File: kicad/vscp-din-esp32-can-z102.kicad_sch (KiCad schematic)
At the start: 39 parts, among them J1 Conn_01x05, J2 Conn_01x02, J3 Conn_01x06, J4 Conn_01x04, J5 Conn_01x04, J6 Conn_01x03, J7 Conn_01x05, J8 Conn_01x02, J9 Conn_01x02, U1 ESP32-C3-WROOM-02-N4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

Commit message: Added code of conduct
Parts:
- U1: DESCRIPTION WiFi Modules (802.11) (Engineering Samples) SMD module, ESP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 -> (none)

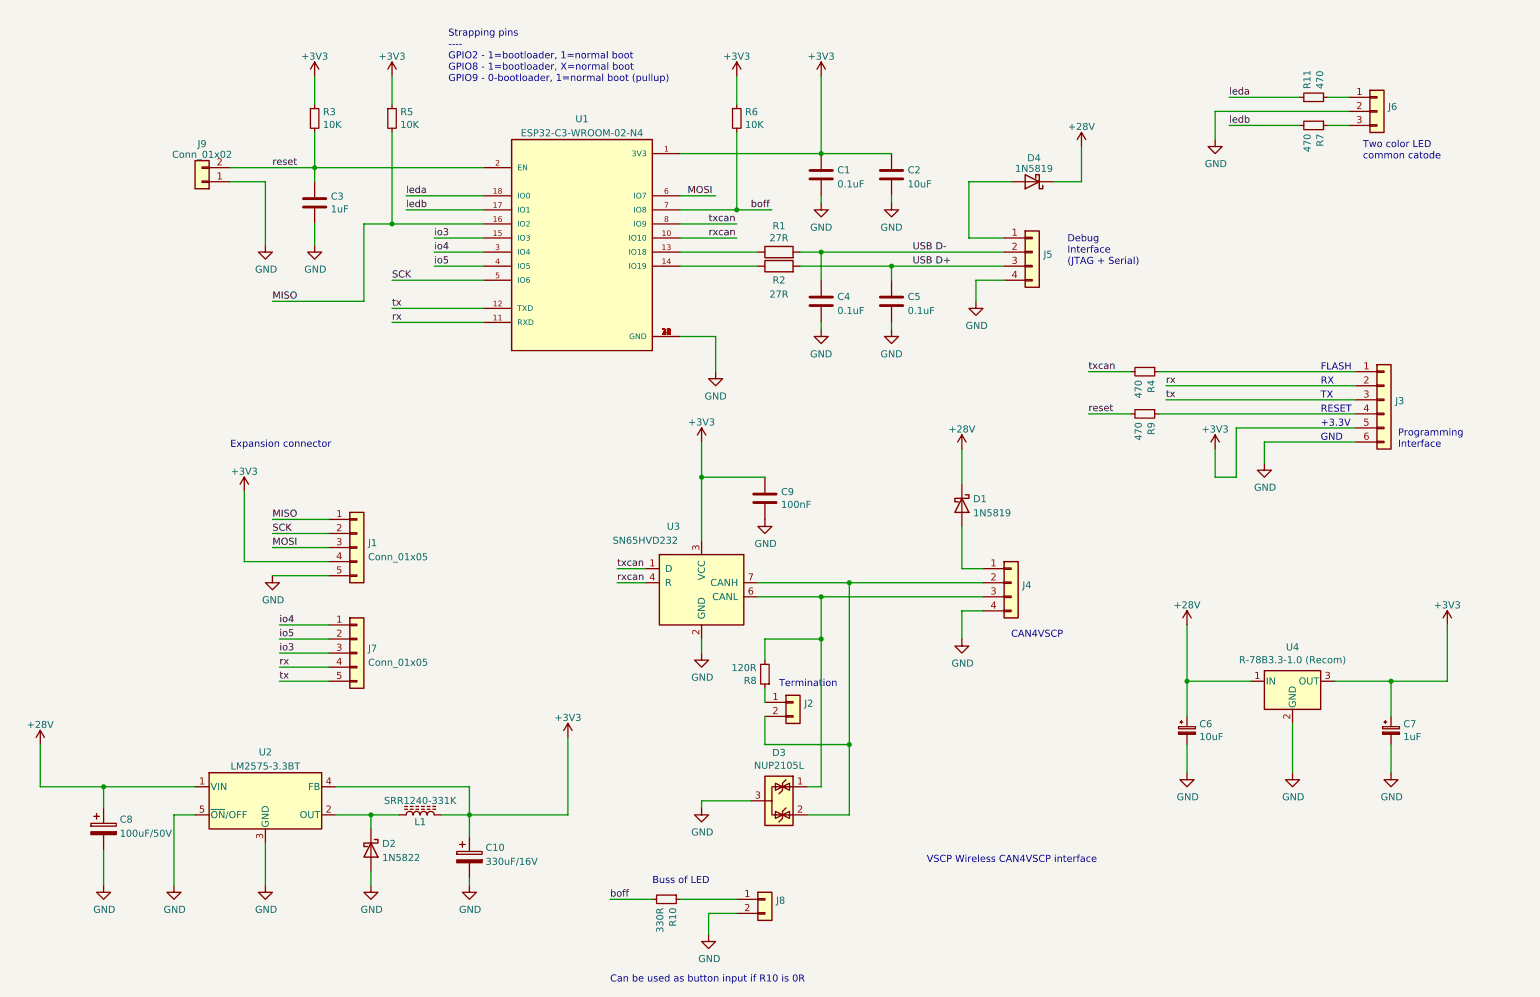
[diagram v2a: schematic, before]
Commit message: Defined status LED colors
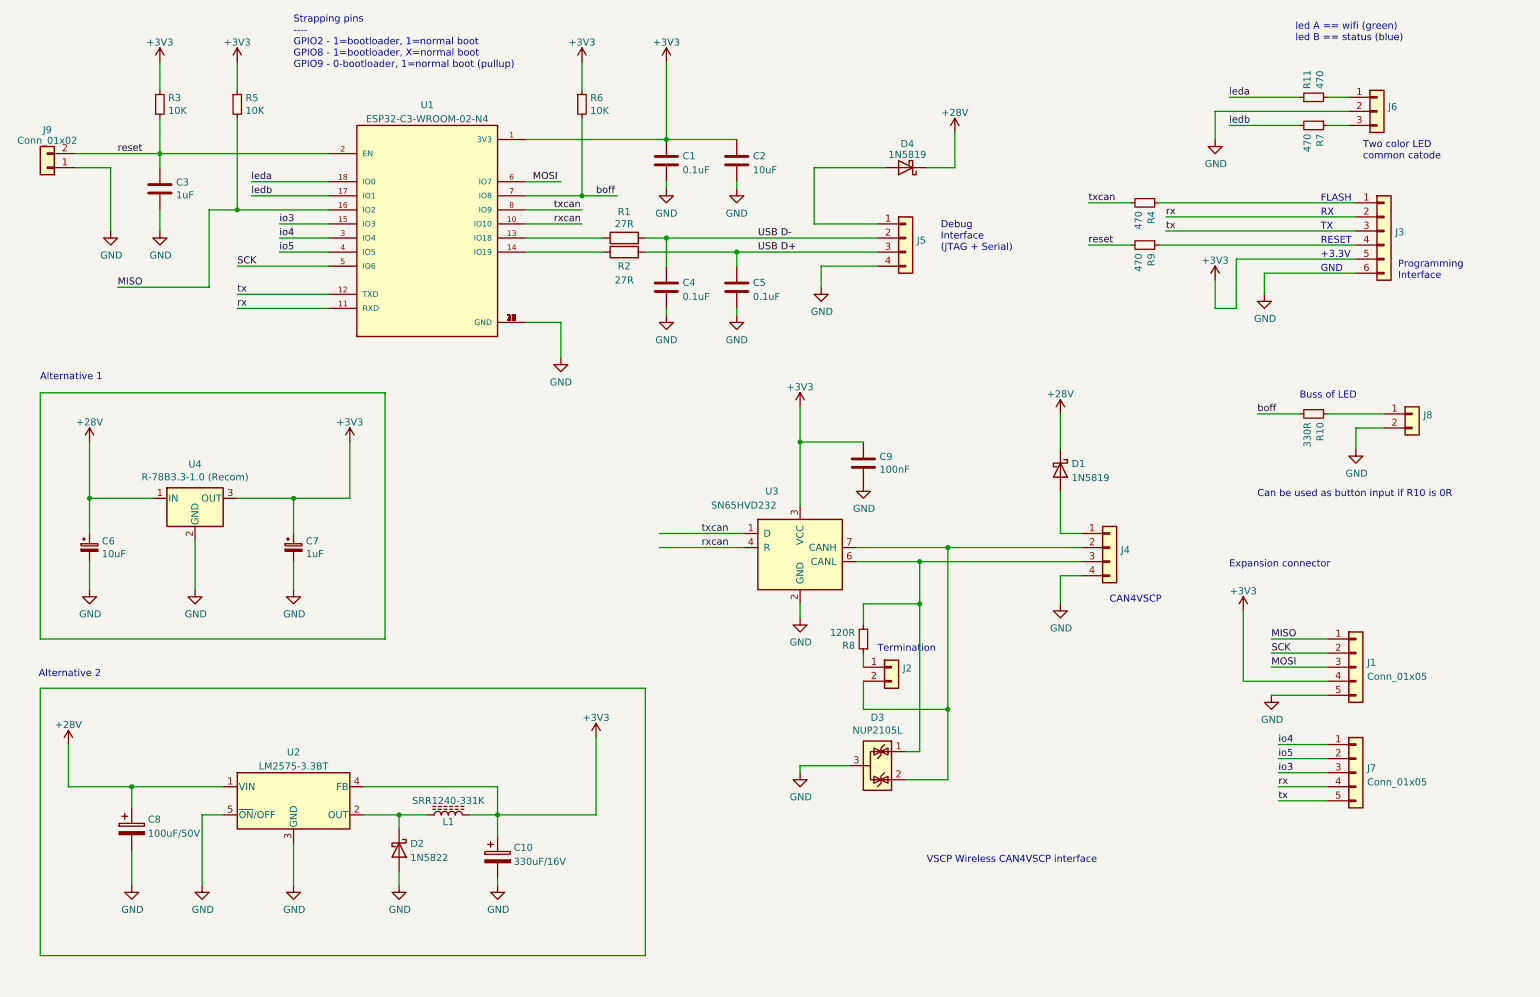
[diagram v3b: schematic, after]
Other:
- note added: "Alternative 1"
- note added: "Alternative 2"
- note added: "led A == wifi (green) led B == status (blue)"
- moved on the sheet: C1, C10, C2, C3, C4, C5, C6, C7, C8, C9, D1, D2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

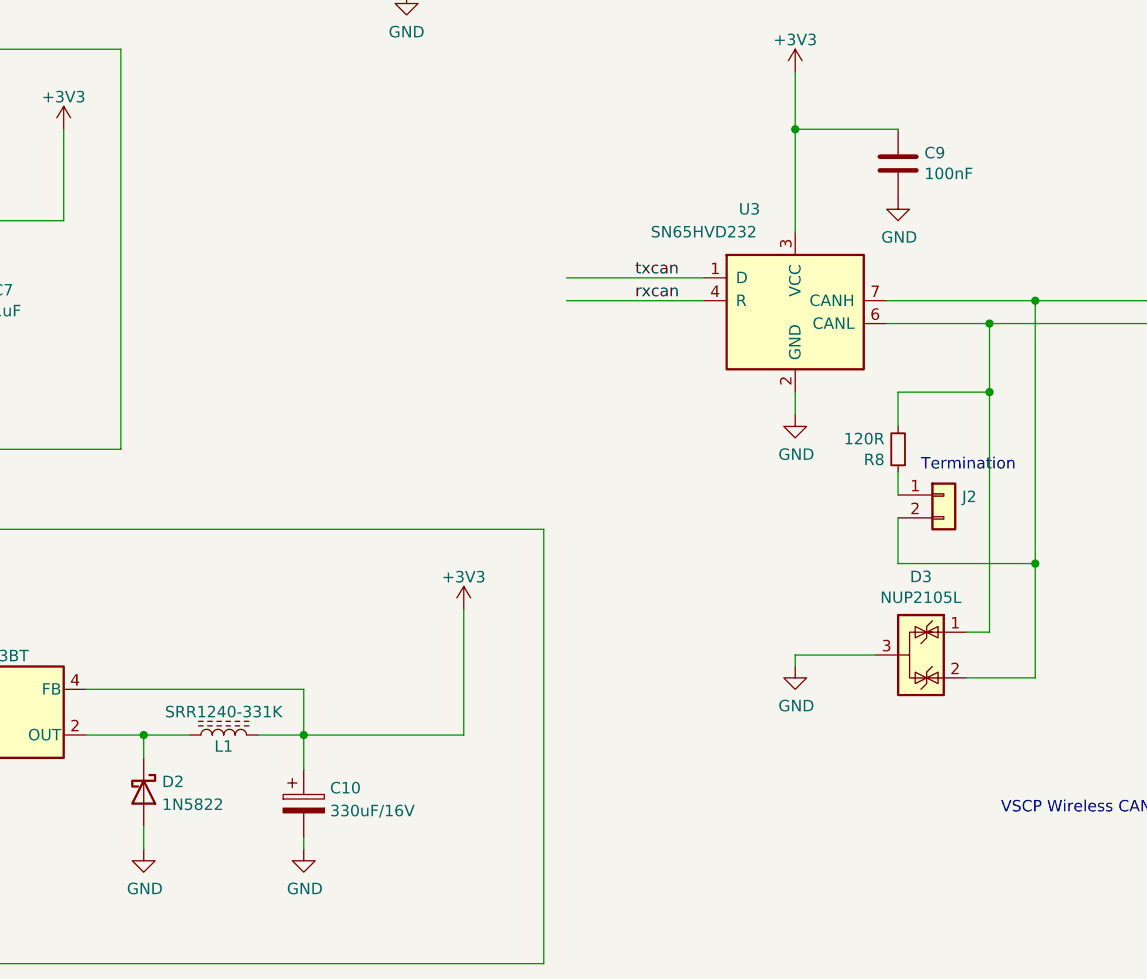
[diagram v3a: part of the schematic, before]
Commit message: Updated schema
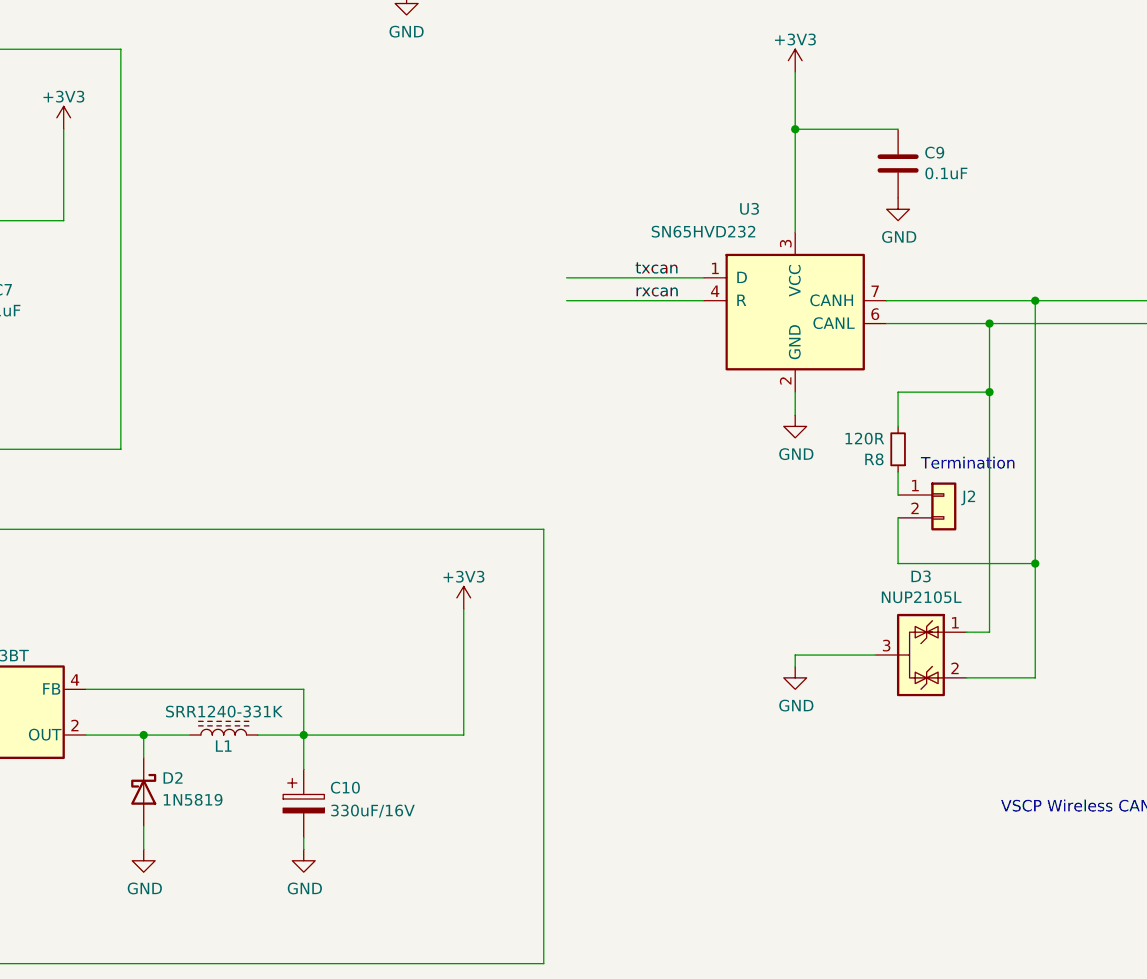
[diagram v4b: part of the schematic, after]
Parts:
- C9: value 100nF -> 0.1uF
- D2: value 1N5822 -> 1N5819
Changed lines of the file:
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@@
 		(fields_autoplaced yes)
 		(property "Reference" "D2"
-			(at 85.852 166.4878 90)
+			(at 85.852 166.1103 90)
 			(show_name no)
 			(do_not_autoplace no)
@@
 			)
 		)
-		(property "Value" "1N5822"
-			(at 85.852 169.0247 90)
+		(property "Value" "1N5819"
+			(at 85.852 168.5346 90)
 			(show_name no)
 			(do_not_autoplace no)
@@
 			)
 		)
-		(property "Value" "100nF"
+		(property "Value" "0.1uF"
 			(at 170.561 98.933 0)
 			(show_name no)
